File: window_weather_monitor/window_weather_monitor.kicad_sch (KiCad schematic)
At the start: 65 parts, among them J1 Barrel_Jack, K1 4x4_Matrix_Keypad, SW1 RST Switch, SW2 PWR DISABLE, U1 Adafruit_Feather_HUZZAH32_ESP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, U2 DHT11, U3 Rain Sensor, U6 LT1086-5.0

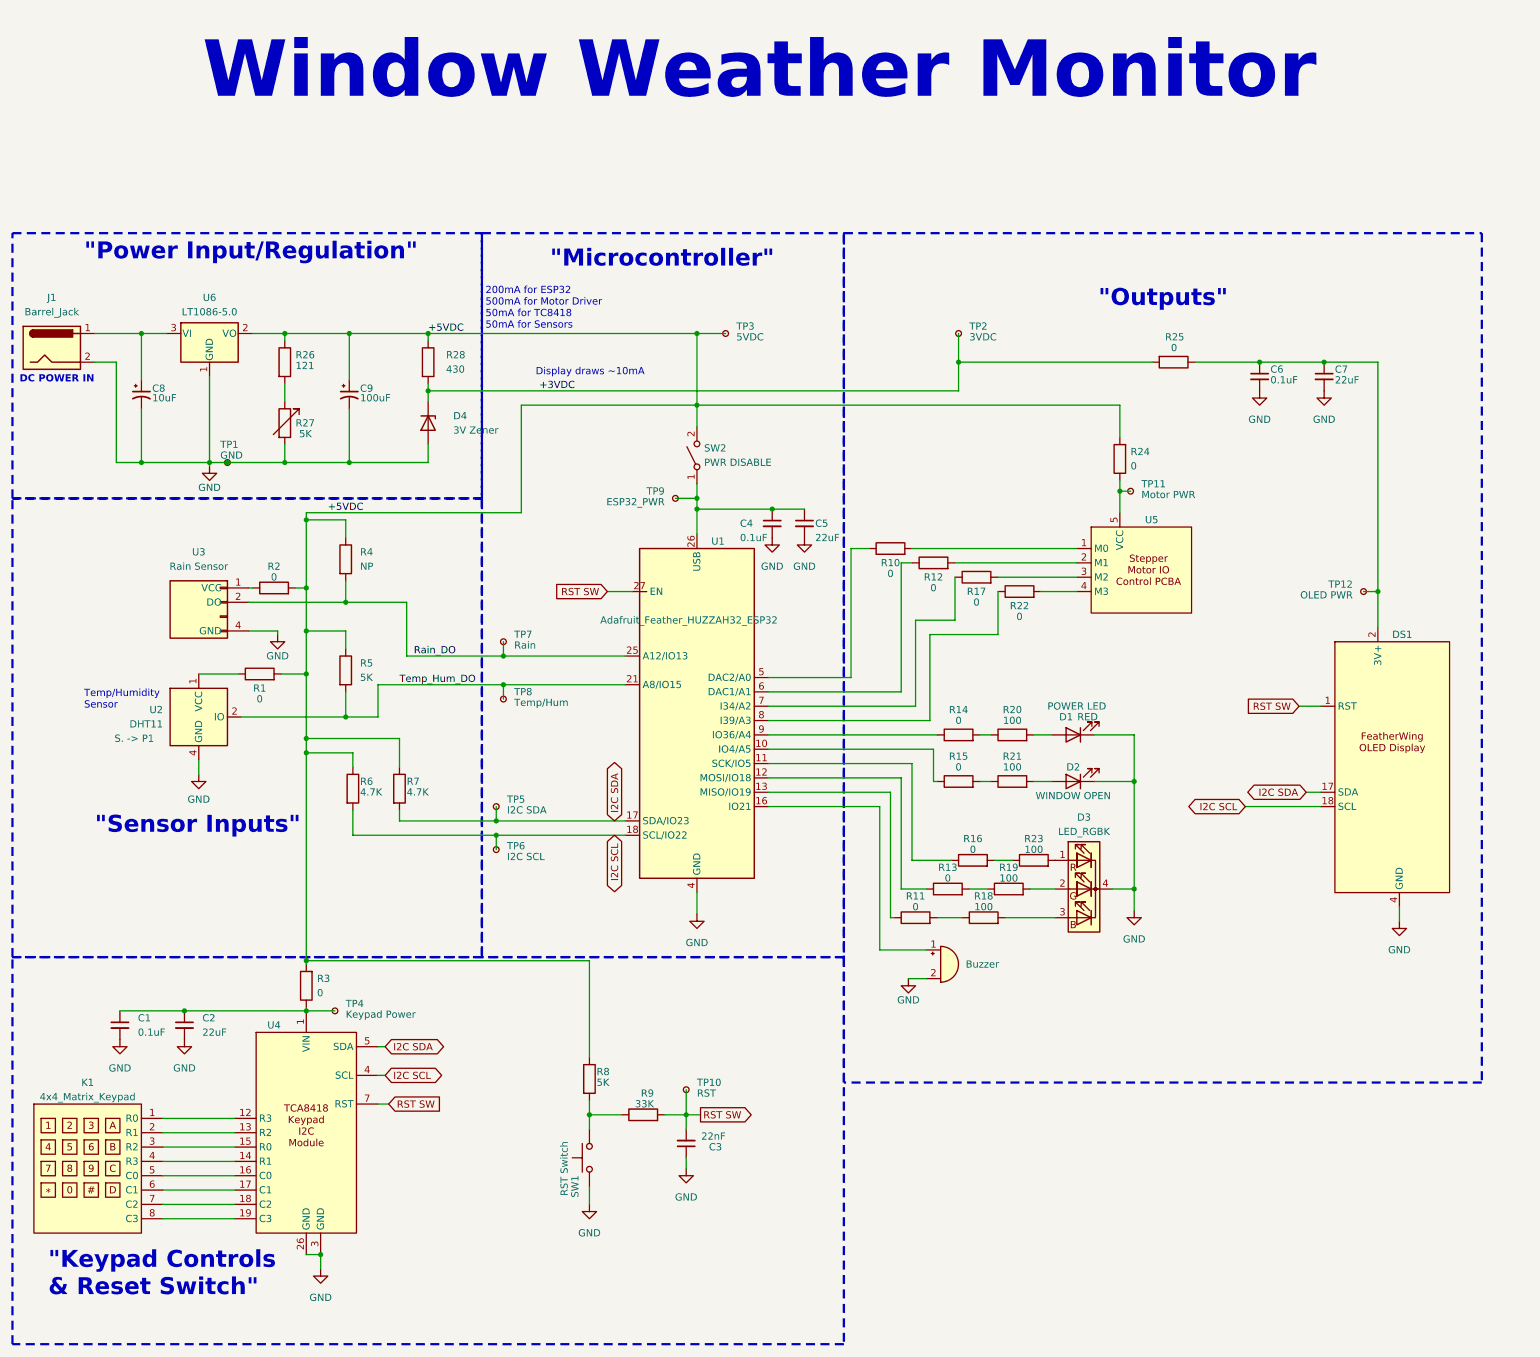
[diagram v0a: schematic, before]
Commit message: Updated PCB
Updated the schematic, layout, generated gerber files for fab, added requisite info on PCB.
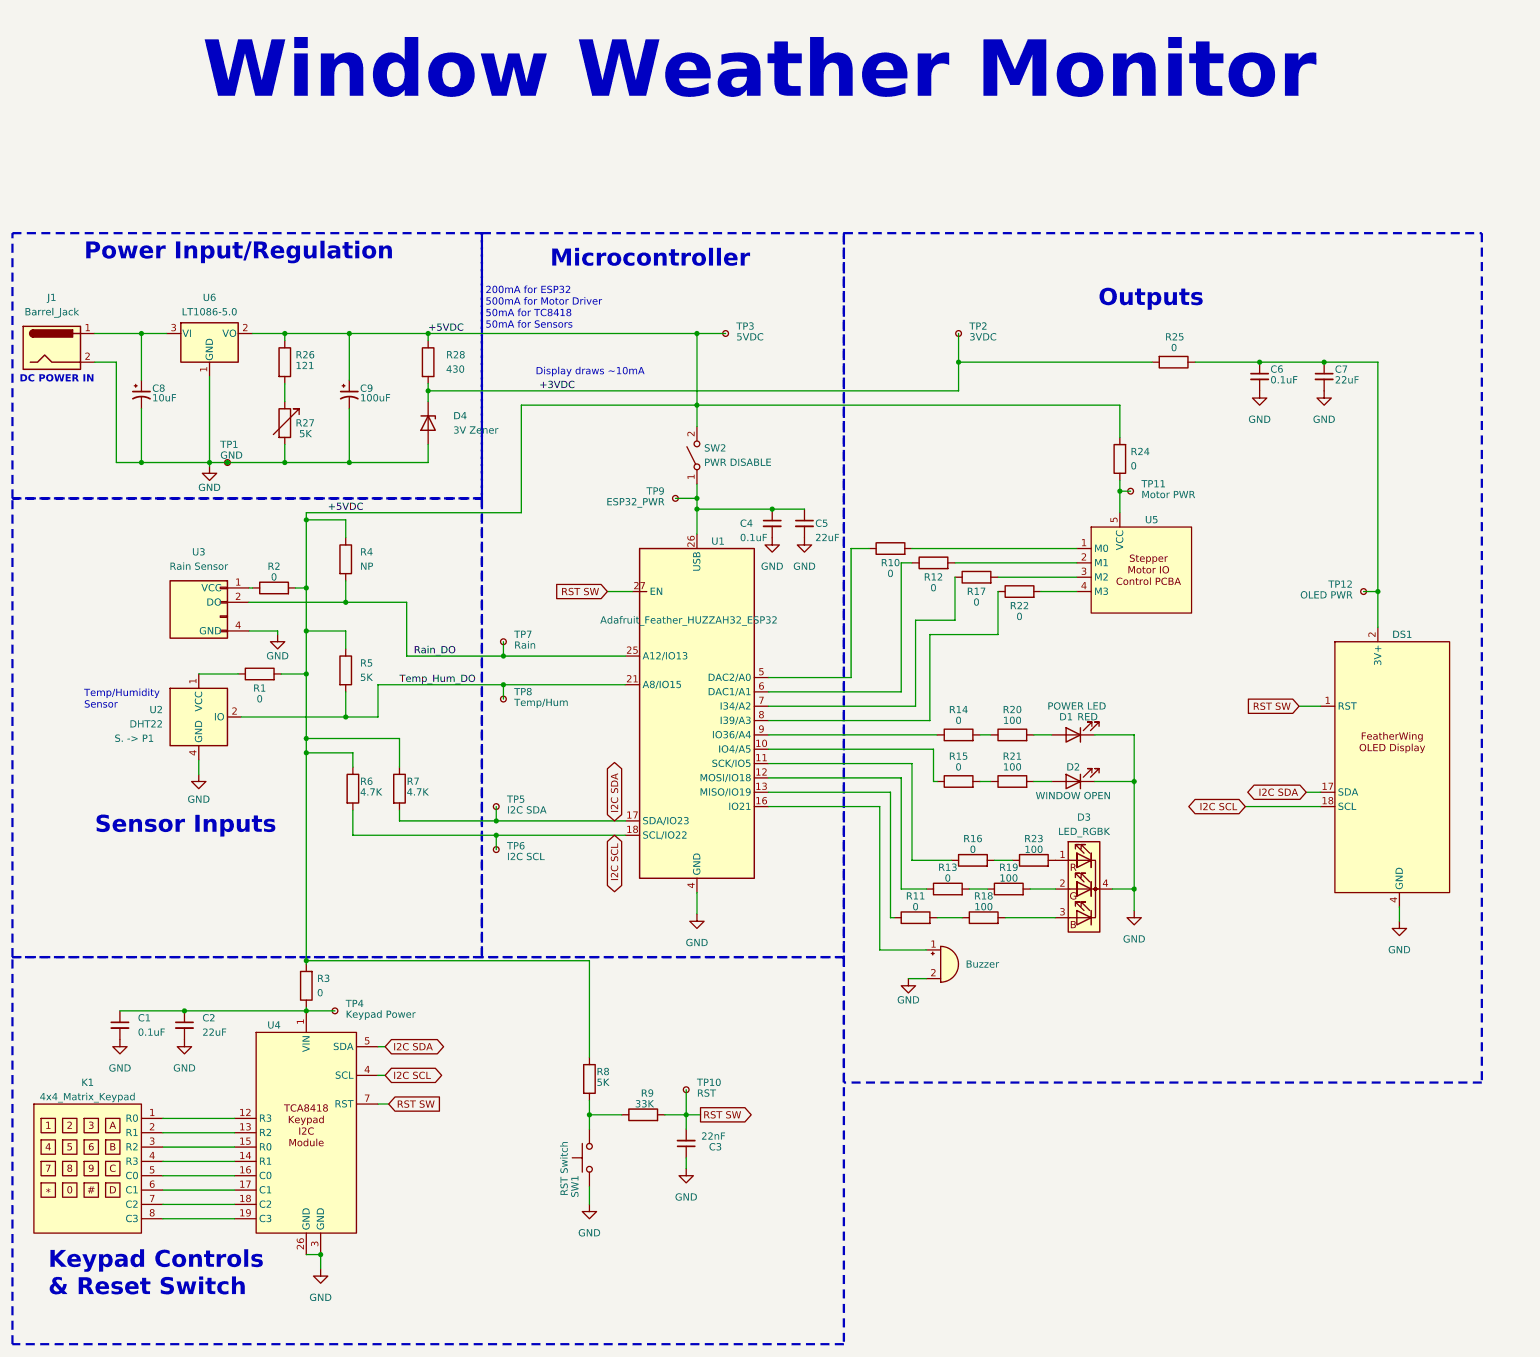
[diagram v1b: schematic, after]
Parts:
- U2: value DHT11 -> DHT22
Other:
- note added: "Keypad Controls & Reset Switch"
- note added: "Microcontroller"
- note added: "Outputs"
- note added: "Power Input/Regulation"
- note added: "Sensor Inputs"
- note removed: ""Keypad Controls & Reset Switch""
- note removed: ""Microcontroller""
- note removed: ""Outputs""
- note removed: ""Power Input/Regulation""
- note removed: ""Sensor Inputs""
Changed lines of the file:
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@@
     (fill (type none))
   )
-  (text "\"Keypad Controls \n& Reset Switch\"" (at 85.725 240.665 0)
+  (text "Keypad Controls\n& Reset Switch" (at 85.725 240.665 0)
     (effects (font (face "KiCad Font") (size 3 3) bold (color 255 76 241 1)) (justify left bottom))
   )
@@
     (effects (font (size 1.27 1.27)) (justify left bottom))
   )
-  (text "\"Microcontroller\"" (at 174.625 58.42 0)
+  (text "Microcontroller" (at 174.625 58.42 0)
     (effects (font (face "KiCad Font") (size 3 3) bold (color 255 76 241 1)) (justify left bottom))
   )
@@
     (effects (font (face "KiCad Font") (size 1.27 1.27) (thickness 0.254) bold) (justify left bottom))
   )
-  (text "\"Sensor Inputs\"" (at 93.98 158.75 0)
+  (text "Sensor Inputs" (at 93.98 158.75 0)
     (effects (font (face "KiCad Font") (size 3 3) bold (color 255 76 241 1)) (justify left bottom))
   )
-  (text "\"Power Input/Regulation\"" (at 92.075 57.15 0)
+  (text "Power Input/Regulation" (at 92.075 57.15 0)
     (effects (font (face "KiCad Font") (size 3 3) bold (color 255 76 241 1)) (justify left bottom))
   )
-  (text "\"Outputs\"" (at 271.78 65.405 0)
+  (text "Outputs" (at 271.78 65.405 0)
     (effects (font (face "KiCad Font") (size 3 3) bold (color 255 76 241 1)) (justify left bottom))
   )
@@
       (effects (font (size 1.27 1.27)) (justify right))
     )
-    (property "Value" "DHT11" (at 106.045 139.065 0)
+    (property "Value" "DHT22" (at 106.045 139.065 0)
       (effects (font (size 1.27 1.27)) (justify right))
     )

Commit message: Changes to make a working board
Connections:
- net GND: now also D3.3 (K); no longer D3.4 (K)
- net at R18.2: now also D3.4 (BA); no longer D3.3 (BA)
- net at R17.1: now also U1.19 (A6/IO14); no longer U1.7 (I34/A2)
- net at R22.1: now also U1.20 (A7/IO32); no longer U1.8 (I39/A3)
- net at U1.22 (A9/IO33): now also R14.1
- net at U1.9 (IO36/A4): no longer R14.1
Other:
- moved on the sheet: D3, R13, R16, R19, R23
